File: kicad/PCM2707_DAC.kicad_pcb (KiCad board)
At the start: 2 copper layers, 49.5 x 37.8 mm, 37 parts, among them CON1 GND_CONNECTORSMD, J1 USB, Q1 12MHz, U1 PCM2707C

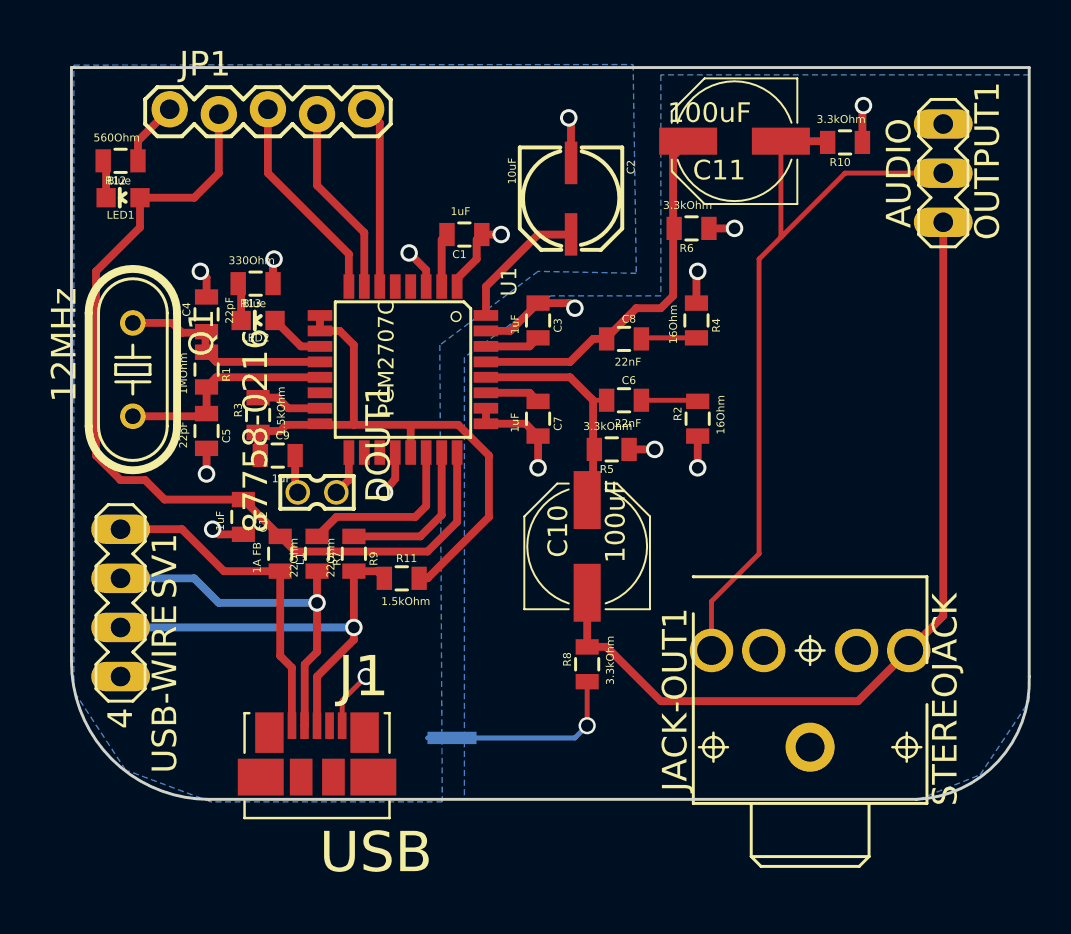
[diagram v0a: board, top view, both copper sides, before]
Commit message: Revert "Rounded corners on design, adding kicad generated berbers"
This reverts commit da9f95aa9fce01ce657d28d8956f70ecfce44641.
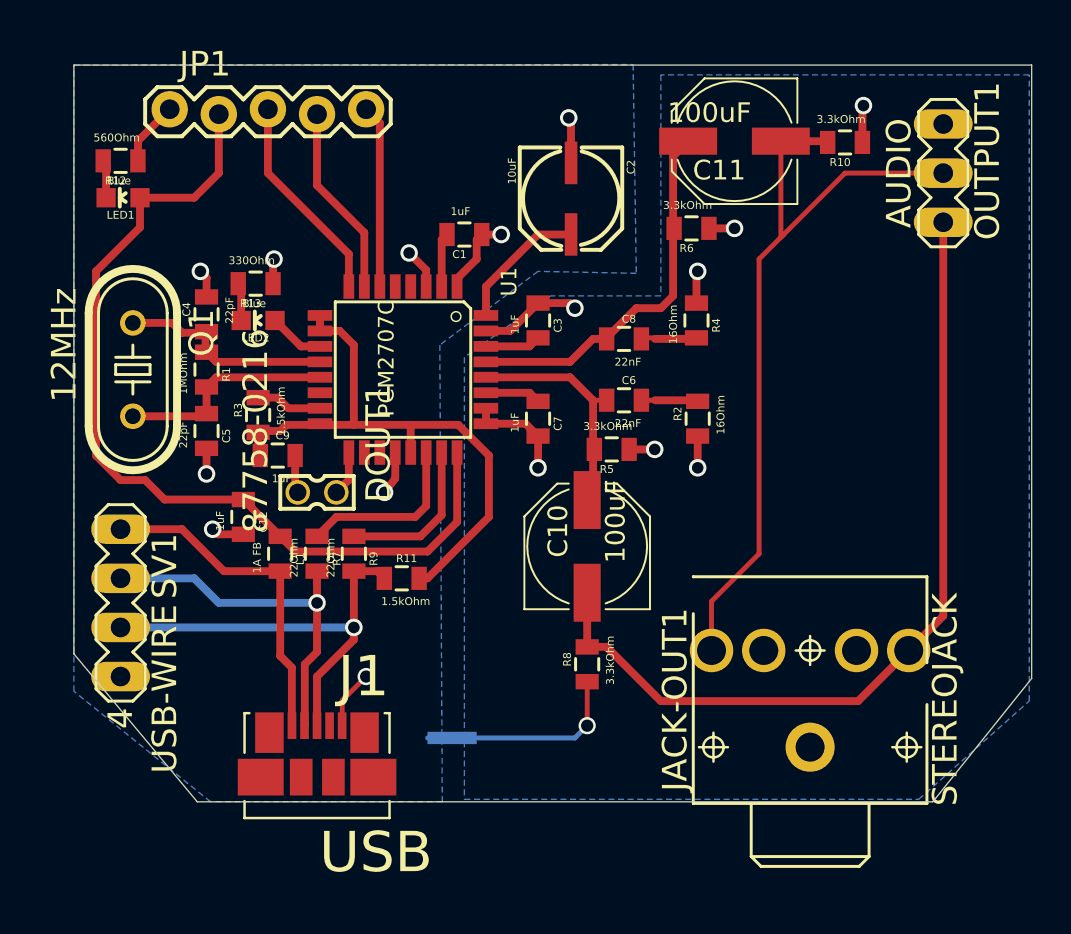
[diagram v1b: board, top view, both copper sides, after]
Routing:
- net /N$18: track 3.01 -> 5.16 mm
- net /N$17: track 2.94 -> 5.04 mm
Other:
- board size 49.5 x 37.8 mm -> 49.5 x 38.1 mm
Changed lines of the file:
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@@
     (links 79)
     (no_connects 0)
-    (area 147.0025 54.7497 198.20029 98.75012)
+    (area 148.704299 55.994299 198.259701 94.119701)
     (thickness 1.6)
     (drawings 6)
-    (tracks 209)
+    (tracks 211)
     (zones 0)
     (modules 37)
@@
     (40 Dwgs.User user)
     (41 Cmts.User user)
-    (42 Eco1.User user hide)
-    (43 Eco2.User user hide)
+    (42 Eco1.User user)
+    (43 Eco2.User user)
     (44 Edge.Cuts user)
   )
@@
     (pad_to_mask_clearance 0.2)
     (aux_axis_origin 0 0)
-    (visible_elements FFFDFFBF)
+    (visible_elements FFFFFFFF)
     (pcbplotparams
-      (layerselection 0x010ec_80000001)
+      (layerselection 0x00030_80000001)
       (usegerberextensions true)
       (excludeedgelayer true)
@@
       (outputformat 1)
       (mirror false)
-      (drillshape 0)
+      (drillshape 1)
       (scaleselection 1)
-      (outputdirectory gerbers/))
+      (outputdirectory ""))
   )
   (net 0 "")
@@
       (net 26 OL))
   )
-  (gr_line (start 198.12 56.134) (end 198.12 87.63) (angle 90) (layer Edge.Cuts) (width 0.15))
-  (gr_line (start 148.59 56.134) (end 198.12 56.134) (angle 90) (layer Edge.Cuts) (width 0.15))
-  (gr_line (start 148.59 86.868) (end 148.59 56.134) (angle 90) (layer Edge.Cuts) (width 0.15))
-  (gr_line (start 192.278 93.98) (end 155.702 93.98) (angle 90) (layer Edge.Cuts) (width 0.15))
-  (gr_arc (start 155.702 86.868) (end 155.702 93.98) (angle 90) (layer Edge.Cuts) (width 0.15))
-  (gr_arc (start 192.024 87.884) (end 198.12 87.63) (angle 90) (layer Edge.Cuts) (width 0.15))
+  (gr_line (start 198.247 56.007) (end 198.247 87.727) (layer Edge.Cuts) (width 0.0254))
+  (gr_line (start 198.247 87.727) (end 193.137 94.107) (layer Edge.Cuts) (width 0.0254))
+  (gr_line (start 193.137 94.107) (end 155.097 94.107) (layer Edge.Cuts) (width 0.0254))
+  (gr_line (start 155.097 94.107) (end 148.717 86.457) (layer Edge.Cuts) (width 0.0254))
+  (gr_line (start 148.717 86.457) (end 148.717 56.007) (layer Edge.Cuts) (width 0.0254))
+  (gr_line (start 148.717 56.007) (end 198.247 56.007) (layer Edge.Cuts) (width 0.0254))
   (segment (start 161.4424 70.555) (end 160.459 70.555) (width 0.4064) (layer Top) (net 1) (status 10))
   (segment (start 160.459 70.555) (end 159.119 69.215) (width 0.4064) (layer Top) (net 1) (status 20))
@@
   (segment (start 170.0276 72.955) (end 172.28 72.955) (width 0.4064) (layer Top) (net 8) (status 10))
   (segment (start 172.28 72.955) (end 172.72 73.395) (width 0.4064) (layer Top) (net 8) (status 20))
-  (segment (start 180.9115 70.11416) (end 178.1175 70.11416) (width 0.254) (layer Top) (net 9) (status 30))
-  (segment (start 178.1175 70.11416) (end 178.06416 70.1675) (width 0.254) (layer Top) (net 9) (status 30))
+  (segment (start 180.9115 70.11416) (end 178.1175 70.11416) (width 0.254) (layer Top) (net 9))
+  (segment (start 178.1175 70.11416) (end 178.06416 70.1675) (width 0.254) (layer Top) (net 9))
+  (segment (start 178.765 70.1675) (end 180.859 70.1675) (width 0.4064) (layer Top) (net 9) (status 30))
   (segment (start 180.859 70.1675) (end 180.9115 70.115) (width 0.4064) (layer Top) (net 9) (status 30))
-  (segment (start 178.06416 73.3425) (end 180.92166 73.3425) (width 0.254) (layer Top) (net 10) (status 30))
-  (segment (start 180.92166 73.3425) (end 180.975 73.39584) (width 0.254) (layer Top) (net 10) (status 30))
+  (segment (start 178.06416 73.3425) (end 180.92166 73.3425) (width 0.254) (layer Top) (net 10))
+  (segment (start 180.92166 73.3425) (end 180.975 73.39584) (width 0.254) (layer Top) (net 10))
+  (segment (start 178.765 73.3425) (end 180.9225 73.3425) (width 0.4064) (layer Top) (net 10) (status 30))
   (segment (start 180.9225 73.3425) (end 180.975 73.395) (width 0.4064) (layer Top) (net 10) (status 30))
   (segment (start 167.735 67.4624) (end 167.735 65.045) (width 0.4064) (layer Top) (net 11) (status 30))
   (segment (start 167.735 65.045) (end 168.01 64.77) (width 0.4064) (layer Top) (net 11) (status 30))
   (segment (start 170.0276 71.355) (end 174.3775 71.355) (width 0.4064) (layer Top) (net 12) (status 10))
-  (segment (start 174.3775 71.355) (end 175.565 70.1675) (width 0.4064) (layer Top) (net 12))
-  (segment (start 175.565 70.1675) (end 176.2125 70.1675) (width 0.4064) (layer Top) (net 12) (status 20))
-  (segment (start 176.2125 70.1675) (end 177.8 68.58) (width 0.4064) (layer Top) (net 12) (status 10))
+  (segment (start 174.3775 71.355) (end 175.565 70.1675) (width 0.4064) (layer Top) (net 12) (status 20))
+  (segment (start 175.565 70.1675) (end 176.2125 70.1675) (width 0.4064) (layer Top) (net 12) (status 10))
+  (segment (start 176.2125 70.1675) (end 177.8 68.58) (width 0.4064) (layer Top) (net 12))
   (segment (start 177.8 68.58) (end 179.07 68.58) (width 0.4064) (layer Top) (net 12))
   (segment (start 179.07 68.58) (end 179.705 67.945) (width 0.4064) (layer Top) (net 12))
@@
   (segment (start 157.365 69.215) (end 157.365 67.46) (width 0.4064) (layer Top) (net 13) (status 30))
   (segment (start 157.365 67.46) (end 157.215 67.31) (width 0.4064) (layer Top) (net 13) (status 30))
-  (segment (start 175.565 73.3425) (end 176.26584 73.3425) (width 0.254) (layer Top) (net 14) (status 20))
+  (segment (start 175.565 73.3425) (end 176.26584 73.3425) (width 0.254) (layer Top) (net 14))
   (segment (start 170.0276 72.155) (end 174.3775 72.155) (width 0.4064) (layer Top) (net 14) (status 10))
-  (segment (start 174.3775 72.155) (end 175.565 73.3425) (width 0.4064) (layer Top) (net 14))
-  (segment (start 175.565 73.3425) (end 175.565 76.2) (width 0.4064) (layer Top) (net 14) (status 20))
+  (segment (start 174.3775 72.155) (end 175.565 73.3425) (width 0.4064) (layer Top) (net 14) (status 20))
+  (segment (start 175.565 73.3425) (end 175.565 76.2) (width 0.4064) (layer Top) (net 14) (status 30))
   (segment (start 175.565 76.2) (end 175.565 78.194) (width 0.4064) (layer Top) (net 14) (status 30))
   (segment (start 175.565 78.194) (end 175.26 78.499) (width 0.4064) (layer Top) (net 14) (status 30))
@@
   (segment (start 167.005 81.165) (end 160.17 81.165) (width 0.4064) (layer Top) (net 23))
   (segment (start 160.17 81.165) (end 159.385 80.38) (width 0.4064) (layer Top) (net 23) (status 20))
-  (segment (start 168.91 90.805) (end 174.625 90.805) (width 0.254) (layer Bottom) (net 24) (status 10))
+  (segment (start 168.91 90.805) (end 174.625 90.805) (width 0.254) (layer Bottom) (net 24))
   (via (at 175.26 90.17) (size 0.889) (drill 0.635) (layers Top Bottom) (net 24))
-  (segment (start 175.26 90.17) (end 175.26 87.89416) (width 0.254) (layer Top) (net 24) (status 20))
+  (segment (start 175.26 90.17) (end 175.26 87.89416) (width 0.254) (layer Top) (net 24))
   (segment (start 174.625 90.805) (end 175.26 90.17) (width 0.254) (layer Bottom) (net 24))
   (via (at 172.72 76.835) (size 0.9048) (drill 0.6) (layers Top Bottom) (net 24))
@@
   (segment (start 189.495 60.0075) (end 189.495 58.155) (width 0.4064) (layer Top) (net 24) (status 10))
   (segment (start 189.495 58.155) (end 189.5475 58.1025) (width 0.4064) (layer Top) (net 24))
-  (segment (start 162.59 90.17) (end 162.59 88.87) (width 0.254) (layer Top) (net 25) (status 10))
+  (segment (start 162.59 90.17) (end 162.59 88.87) (width 0.254) (layer Top) (net 25))
   (via (at 163.83 87.63) (size 0.889) (drill 0.635) (layers Top Bottom) (net 25))
   (segment (start 162.59 88.87) (end 163.83 87.63) (width 0.254) (layer Top) (net 25))
-  (segment (start 167.005 90.805) (end 167.64 90.805) (width 0.254) (layer Bottom) (net 25) (status 30))
+  (segment (start 167.005 90.805) (end 167.64 90.805) (width 0.254) (layer Bottom) (net 25))
   (via (at 164.7825 78.105) (size 0.9048) (drill 0.6) (layers Top Bottom) (net 25))
   (via (at 166.0525 65.7225) (size 0.9048) (drill 0.6) (layers Top Bottom) (net 25))
@@
       (pts
         (xy 148.717 56.007) (xy 177.636494 55.980006) (xy 177.8 66.775006) (xy 172.72 66.675) (xy 167.64 70.485)
-        (xy 167.767 94.107) (xy 155.785991 94.107) (xy 151.384 92.456) (xy 148.717 88.392)
+        (xy 167.767 94.107) (xy 155.785991 94.107) (xy 148.717 88.392)
       )
     )
@@
     (polygon
       (pts
-        (xy 168.91 93.98) (xy 192.405 93.98) (xy 195.58 92.71) (xy 198.12 88.9) (xy 198.12 56.515)
-        (xy 179.07 56.515) (xy 179.07 67.945) (xy 173.355 67.945) (xy 168.91 71.12)
+        (xy 168.91 93.98) (xy 192.405 93.98) (xy 198.12 88.9) (xy 198.12 56.515) (xy 179.07 56.515)
+        (xy 179.07 67.945) (xy 173.355 67.945) (xy 168.91 71.12)
       )
     )
